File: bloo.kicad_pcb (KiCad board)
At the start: 2 copper layers, 90 x 96 mm, 89 parts, among them J5 SWD_Header, M1 M1_Conn_Alt, M2 M2_Conn_Alt, Q0 TEFT4300, Q1 TEFT4300, Q10 Q_NMOS_GSD, Q11 Q_NMOS_GSD, Q12 Q_NMOS_GSD, Q2 TEFT4300, Q3 TEFT4300, Q9 Q_NMOS_GSD, SW1 SW, SW2 SW, SW3 SW, U1 YAAJ_BluePill_SWD_Breakout, U2 L293D, U3 LM1085-5.0, U4 APE8865Y5-33-HF-3, U5 BC832

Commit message: fixing DRC errors
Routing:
- net +5V: track 240.4 -> 244.8 mm
- net GND: track 0.00 -> 0.07 mm, vias 100 -> 106
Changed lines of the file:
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@@
 		(net 1)
 	)
+	(segment
+		(start 297.12 123.98)
+		(end 297.17 124.03)
+		(width 0.5)
+		(layer "F.Cu")
+		(net 2)
+	)
 	(via
 		(at 248.12 60.82)
@@
 	)
 	(via
+		(at 296.99 127.98)
+		(size 0.6)
+		(drill 0.3)
+		(layers "F.Cu" "B.Cu")
+		(free yes)
+		(net 2)
+	)
+	(via
 		(at 211.140994 76.548206)
 		(size 0.7)
@@
 	)
 	(via
-		(at 297.16 123.27)
-		(size 0.6)
-		(drill 0.3)
+		(at 268.38 98.86)
+		(size 0.8)
+		(drill 0.4)
 		(layers "F.Cu" "B.Cu")
 		(free yes)
@@
 	)
 	(via
-		(at 297.88 134.01)
-		(size 0.6)
-		(drill 0.3)
+		(at 293.56 65.59)
+		(size 0.8)
+		(drill 0.4)
 		(layers "F.Cu" "B.Cu")
 		(free yes)
@@
 	)
 	(via
-		(at 268.38 98.86)
-		(size 0.8)
+		(at 260.46 40.72)
+		(size 0.7)
 		(drill 0.4)
 		(layers "F.Cu" "B.Cu")
@@
 	)
 	(via
-		(at 293.56 65.59)
+		(at 259.36 100.81)
 		(size 0.8)
 		(drill 0.4)
@@
 	)
 	(via
-		(at 260.46 40.72)
-		(size 0.7)
-		(drill 0.4)
+		(at 282.34 134.39)
+		(size 0.6)
+		(drill 0.3)
 		(layers "F.Cu" "B.Cu")
 		(free yes)
@@
 	)
 	(via
-		(at 259.36 100.81)
-		(size 0.8)
-		(drill 0.4)
+		(at 280.67 131.06)
+		(size 0.6)
+		(drill 0.3)
 		(layers "F.Cu" "B.Cu")
 		(free yes)
@@
 	)
 	(via
+		(at 280.7 128.04)
+		(size 0.6)
+		(drill 0.3)
+		(layers "F.Cu" "B.Cu")
+		(free yes)
+		(net 2)
+	)
+	(via
 		(at 250.27 104.58)
 		(size 0.8)
@@
 	)
 	(via
+		(at 298.5 134.21)
+		(size 0.6)
+		(drill 0.3)
+		(layers "F.Cu" "B.Cu")
+		(free yes)
+		(net 2)
+	)
+	(via
 		(at 275.32 113.58)
 		(size 0.8)
@@
 	)
 	(via
+		(at 281.56 129.5)
+		(size 0.6)
+		(drill 0.3)
+		(layers "F.Cu" "B.Cu")
+		(free yes)
+		(net 2)
+	)
+	(via
 		(at 282.36 88.78)
 		(size 0.8)
@@
 	)
 	(via
+		(at 281.76 133.53)
+		(size 0.6)
+		(drill 0.3)
+		(layers "F.Cu" "B.Cu")
+		(free yes)
+		(net 2)
+	)
+	(via
+		(at 297.01 129)
+		(size 0.6)
+		(drill 0.3)
+		(layers "F.Cu" "B.Cu")
+		(free yes)
+		(net 2)
+	)
+	(via
 		(at 282.536857 100.107682)
 		(size 0.8)
@@
 	)
 	(via
+		(at 297.46 133.51)
+		(size 0.6)
+		(drill 0.3)
+		(layers "F.Cu" "B.Cu")
+		(free yes)
+		(net 2)
+	)
+	(via
 		(at 214.82 71.04)
 		(size 0.6)
@@
 	)
 	(via
-		(at 246.48 134.14)
-		(size 0.7)
-		(drill 0.4)
+		(at 297.12 123.09)
+		(size 0.6)
+		(drill 0.3)
 		(layers "F.Cu" "B.Cu")
 		(free yes)
@@
 	)
 	(via
-		(at 224.86 131.4)
+		(at 246.48 134.14)
 		(size 0.7)
 		(drill 0.4)
@@
 	)
 	(via
-		(at 293.42 123.83)
-		(size 0.6)
-		(drill 0.3)
+		(at 224.86 131.4)
+		(size 0.7)
+		(drill 0.4)
 		(layers "F.Cu" "B.Cu")
 		(free yes)
@@
 	)
 	(via
-		(at 297.14 133.36)
-		(size 0.6)
-		(drill 0.3)
-		(layers "F.Cu" "B.Cu")
-		(free yes)
-		(net 2)
-	)
-	(via
 		(at 253.39 127.61)
 		(size 0.8)
@@
 	)
 	(segment
+		(start 217.507626 67.412374)
+		(end 216.71 68.21)
+		(width 1.5)
+		(layer "F.Cu")
+		(net 4)
+	)
+	(segment
 		(start 216.776626 63.424)
 		(end 217.507626 64.155)
@@
 	)
 	(segment
+		(start 217.507626 64.155)
+		(end 217.507626 67.412374)
+		(width 1.5)
+		(layer "F.Cu")
+		(net 4)
+	)
+	(segment
 		(start 213.869 70.386082)
 		(end 216.045082 68.21)
@@
 		(polygon
 			(pts
-				(xy 287.87 134.81) (xy 287.87 130.76) (xy 298.73 130.76) (xy 298.65 134.8) (xy 298.66 134.8)
+				(xy 287.81 134.44) (xy 287.87 130.76) (xy 296.51 130.84) (xy 296.41 134.32) (xy 296.4 134.43)
 			)
 		)

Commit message: clearing drc errors
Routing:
- net GND: track 0.07 -> 12.8 mm, vias 106 -> 108
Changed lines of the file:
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@@
+	)
+	(segment
+		(start 284.7985 134.475)
+		(end 283.9225 133.599)
+		(width 0.3)
+		(layer "F.Cu")
+		(net 2)
 	)
 	(segment
@@
 		(net 2)
 	)
+	(segment
+		(start 295.5435 134.153546)
+		(end 295.222046 134.475)
+		(width 0.3)
+		(layer "F.Cu")
+		(net 2)
+	)
+	(segment
+		(start 295.5435 133.825)
+		(end 295.5435 134.153546)
+		(width 0.3)
+		(layer "F.Cu")
+		(net 2)
+	)
+	(segment
+		(start 295.222046 134.475)
+		(end 284.7985 134.475)
+		(width 0.3)
+		(layer "F.Cu")
+		(net 2)
+	)
+	(segment
+		(start 295.3275 133.609)
+		(end 295.5435 133.825)
+		(width 0.3)
+		(layer "F.Cu")
+		(net 2)
+	)
 	(via
 		(at 248.12 60.82)
@@
 	)
 	(via
+		(at 293.43 123.72)
+		(size 0.6)
+		(drill 0.3)
+		(layers "F.Cu" "B.Cu")
+		(free yes)
+		(net 2)
+	)
+	(via
 		(at 280.67 131.06)
 		(size 0.6)
@@
 		(layers "F.Cu" "B.Cu")
 		(free yes)
+		(net 2)
+	)
+	(via
+		(at 294.1 127.57)
+		(size 0.7)
+		(drill 0.3)
+		(layers "F.Cu" "B.Cu")
+		(free yes)

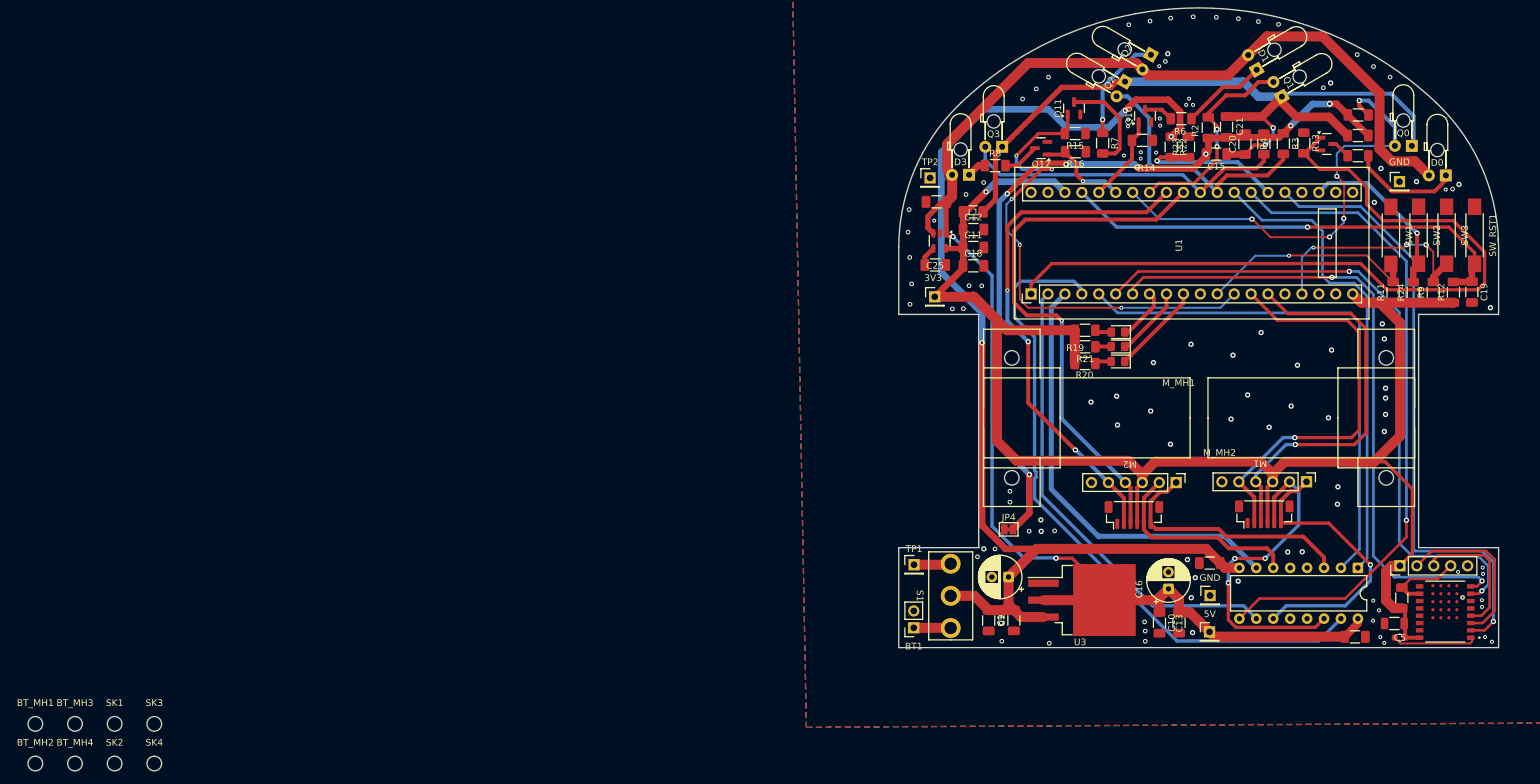
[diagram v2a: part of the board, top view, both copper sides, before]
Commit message: silkscreen done
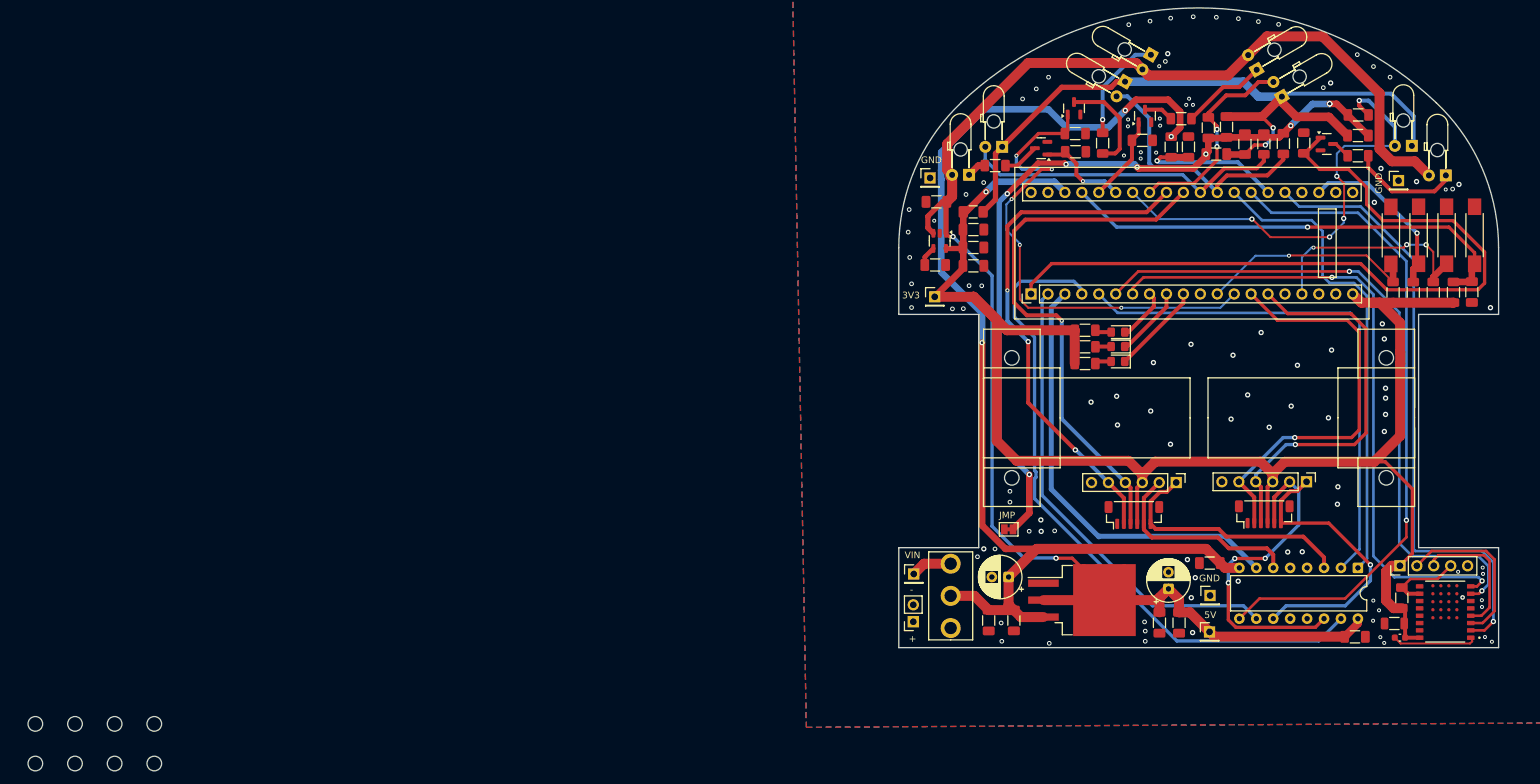
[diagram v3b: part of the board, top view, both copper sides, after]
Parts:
- moved TP1 1.39 mm to (211.8, 124.0)
- moved BT1 0.92 mm to (211.7, 131.2)
- moved GND 0.21 mm to (284.5, 65.0)
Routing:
- net Net-(BT1-+): track 5.55 -> 0.04 mm
- net Net-(S1-Pad3): track 5.56 -> 6.18 mm
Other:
- board text added: "+"
- board text added: "-"
- board text added: "3V3"
- board text added: "5V"
- board text added: "GND"
- board text added: "JMP"
- board text added: "VIN"

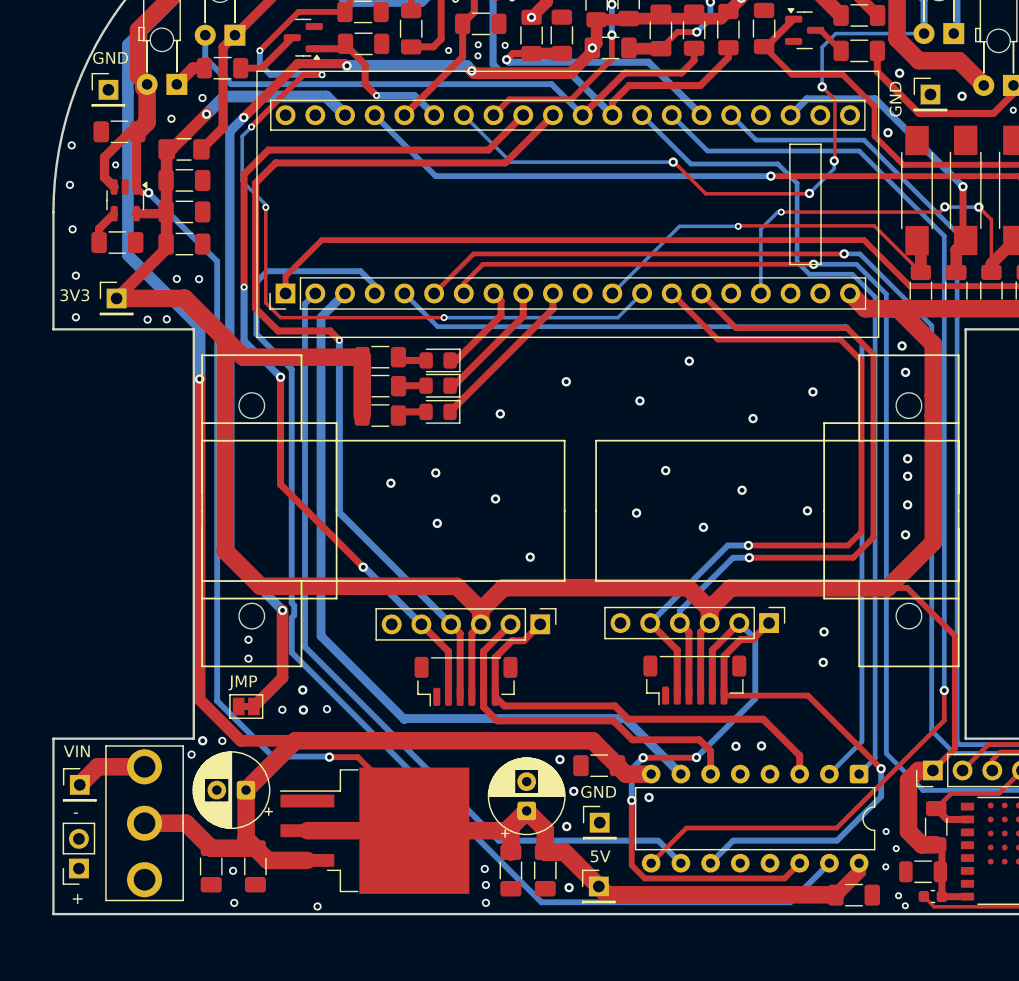
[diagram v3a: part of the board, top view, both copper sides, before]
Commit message: green board --> connector footprint + logo
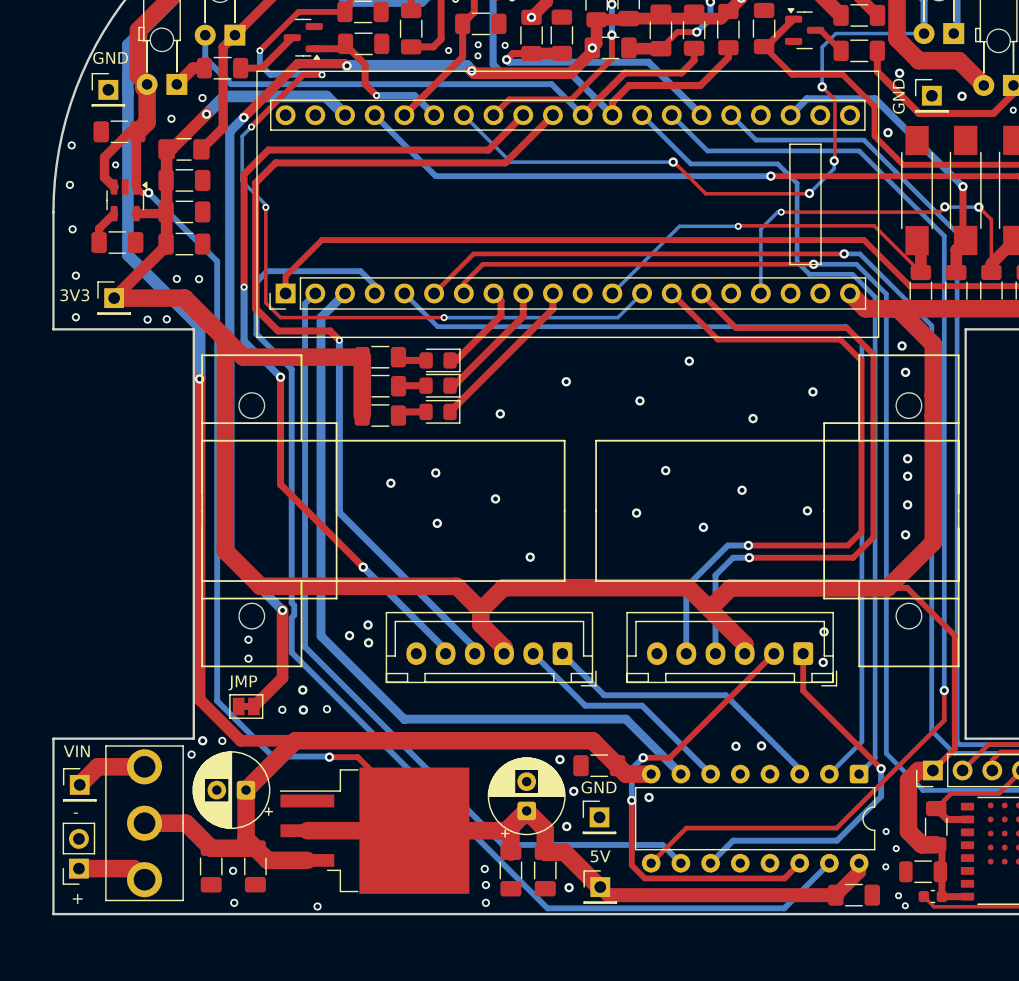
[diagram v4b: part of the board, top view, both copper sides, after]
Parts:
- removed 3V3: TP_3V3, Connector_PinHeader_2.54mm:PinHeader_1x01_P2.54mm_Vertical
- removed 5V: TP_5V, Connector_PinHeader_2.54mm:PinHeader_1x01_P2.54mm_Vertical
- removed GND (x2): GND_TP, Connector_PinHeader_2.54mm:PinHeader_1x01_P2.54mm_Vertical
- added G***: LOGO, LOGO, B.Cu at (254.6, 94.9)
- added TP3: TP_5V, Connector_PinHeader_2.54mm:PinHeader_1x01_P2.54mm_Vertical, F.Cu at (256.3, 132.8)
- added TP4: TP_3V3, Connector_PinHeader_2.54mm:PinHeader_1x01_P2.54mm_Vertical, F.Cu at (214.7, 82.4)
- added TP5: GND_TP, Connector_PinHeader_2.54mm:PinHeader_1x01_P2.54mm_Vertical, F.Cu at (284.6, 65.1)
- added TP6: GND_TP, Connector_PinHeader_2.54mm:PinHeader_1x01_P2.54mm_Vertical, F.Cu at (256.2, 126.8)
- M1, M2: footprint MM_Library:Motor Headers -> Connector_JST:JST_XH_B6B-XH-A_1x06_P2.50mm_Vertical
- moved M1 11.5 mm to (273.6, 112.8)
- moved M2 10.6 mm to (253.0, 112.8)
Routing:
- net M1_OUT_1: track 38.1 -> 24.8 mm
- net M2_OUT_1: track 43.7 -> 31.9 mm
- net M1_OUT_2: track 31.0 -> 19.4 mm
- net M2_OUT_2: track 50.9 -> 39.8 mm, vias 3 -> 2
- net +3V3: track 243.6 -> 237.2 mm
- net Net-(BT1-+): track 0.04 -> 6.00 mm
- net M2_ENC_B: track 61.7 -> 55.9 mm
- net M2_ENC_A: track 59.2 -> 54.1 mm
- net M1_ENC_B: track 77.9 -> 74.3 mm
- net M1_ENC_A: track 81.6 -> 78.4 mm
- net GND: vias 108 -> 111

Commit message: BOM Complete
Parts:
- R1, R2, R3, R4: value 1.8k -> 1.8K
- R10: value 10k -> 10K
- R5, R6, R7, R8: value 35 -> 36
- U4: value APE8865Y5-33-HF-3 -> NCP161ASN330T1G
- moved BT_MH2 83.3 mm to (136.2, 91.1)
- moved BT_MH4 83.3 mm to (142.2, 91.1)
- moved SK2 83.3 mm to (148.1, 91.1)
- moved SK4 83.3 mm to (154.1, 91.1)
- moved BT_MH3 83.3 mm to (142.2, 85.2)
- moved SK3 83.3 mm to (154.1, 85.2)
- moved BT_MH1 83.3 mm to (136.2, 85.2)
- moved SK1 83.3 mm to (148.1, 85.2)

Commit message: Gerber and Pos files generated (+drl files)
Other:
- rule pad_to_mask_clearance: 0.2 -> 0
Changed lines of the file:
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@@
 			(dielectric_constraints no)
 		)
-		(pad_to_mask_clearance 0.2)
-		(solder_mask_min_width 0.25)
+		(pad_to_mask_clearance 0)
 		(allow_soldermask_bridges_in_footprints no)
 		(tenting front back)

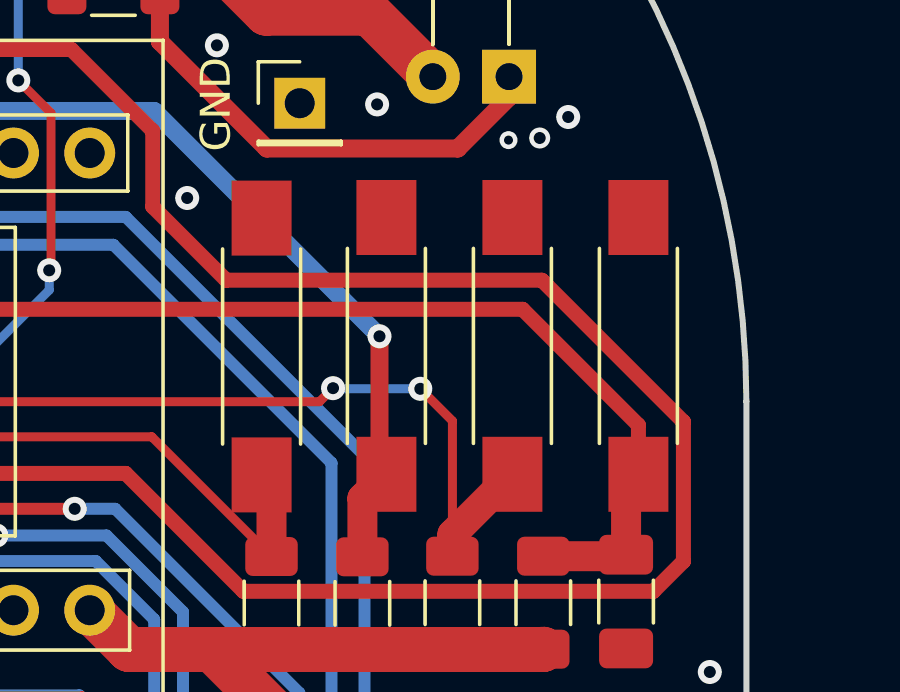
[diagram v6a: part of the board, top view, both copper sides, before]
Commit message: updated button footprint
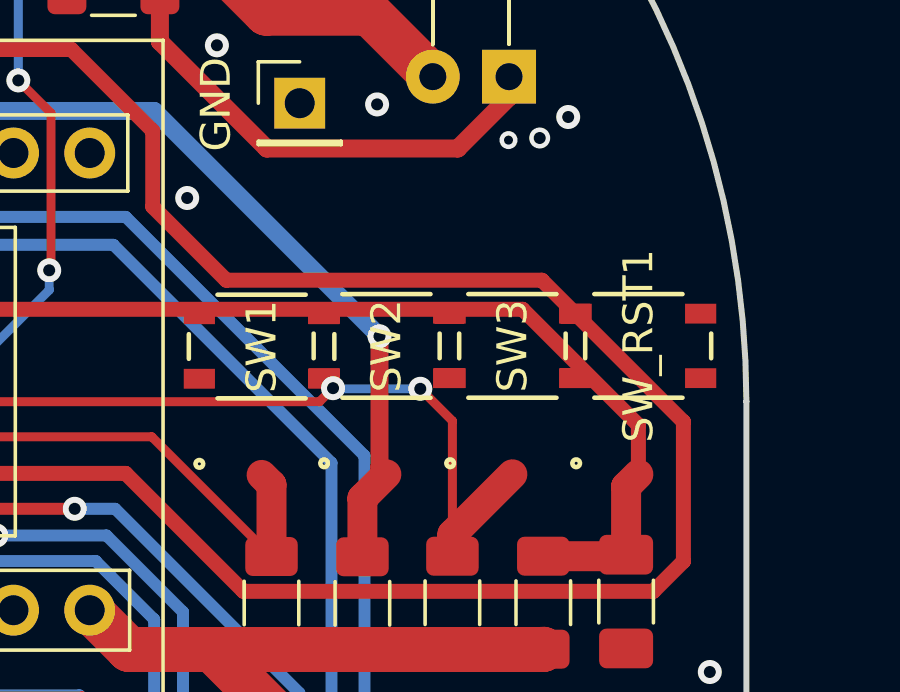
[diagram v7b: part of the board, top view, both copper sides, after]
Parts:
- SW1, SW2, SW3, SW_RST1: footprint Button_Switch_SMD:SW_SPST_REED_CT05-XXXX-G1 -> MM_Library:SW4_SKRPABE010_ALPS
